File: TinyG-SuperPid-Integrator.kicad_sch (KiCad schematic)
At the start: 16 parts, among them J1 TINYG, J2 SPP, J3 Vin (12-26V), U1 LM2678T-5.0

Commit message: Completed schematic, first Rev of PCB layout complete.
PCB Layout complete
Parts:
- added C2: .1uF, Capacitor_THT:C_Disc_D3.8mm_W2.6mm_P2.50mm, symbol Device:C_Small
- added J4: UJ2-AH-4-TH, 1_MyGlobalLibFootprintLibrary:CUI_UJ2-AH-4-TH, symbol 1_MyGlobalLib:UJ2-AH-4-TH
- added J5: SSR, 1_MyGlobalLibFootprintLibrary:CUI_TB001-500-02BE, symbol 1_MyGlobalLib:TB001-500-02BE
- added R5, R7: 47K, 1_MyGlobalLibFootprintLibrary:MRS25000C2260FCT00, symbol Device:R_Small_US
- added R6: 82K, 1_MyGlobalLibFootprintLibrary:MRS25000C2260FCT00, symbol Device:R_Small_US
- added R8: 38.3K, 1_MyGlobalLibFootprintLibrary:MRS25000C2260FCT00, symbol Device:R_Small_US
- added R9: 226, 1_MyGlobalLibFootprintLibrary:MRS25000C2260FCT00, symbol Device:R_Small_US
- added U3: TLP2662F, 1_MyGlobalLibFootprintLibrary:TLP2662F, symbol 1_MyGlobalLib:TLP2662F
- gave numbers to parts that had none: 1
- renumbered Cb to Cb1, Cin to Cin1, Cinx to Cinx1, Cout to Cout1
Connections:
- net +5V: now also C2.1, J4.1 (Vcc), R6.2, R8.2, U3.8 (Vcc)
- net GND: now also C2.2, J4.4 (GND), J4.5 (SHIELD), J5.2 (-), R5.1, R7.1, R9.1, U3.5 (GND)
- net at J1.3 (COOL): now also U3.4 (A2)
- new net: J4.2 (D-), R5.2, R6.1
- new net: J4.3 (D+), R7.2, R8.1
- new net: J5.1 (+), U3.6 (O2)
- new net: R9.2, U3.3 (C2)
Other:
- note added: "TinyG and SuperPID integration. Converts 3.3V TinyG outputs to 5.0 volt levels. Inverts SPIN command from active low to active high. Has solid state relay output for external actuation of cooling or dust collection. Includes 5V, 4Amp power supply with USB Output for Raspberry pi or other small USB device. Provides 5V power for SuperPID."
- note removed: "TinyG and SuperPID integration. Converts 3.3V TinyG outputs to 5.0 volt levels. Inverts SPIN command from active low to active high. Has relay output for external actuation of cooling or dust collection. Includes 5V, 4Amp power supply with USB Output for Raspberry pi or other small USB device. Provieds 5V power for SuperPID."
- moved on the sheet: Cb1, Cin1, Cinx1, Cout1, D1, J3, L1, U1

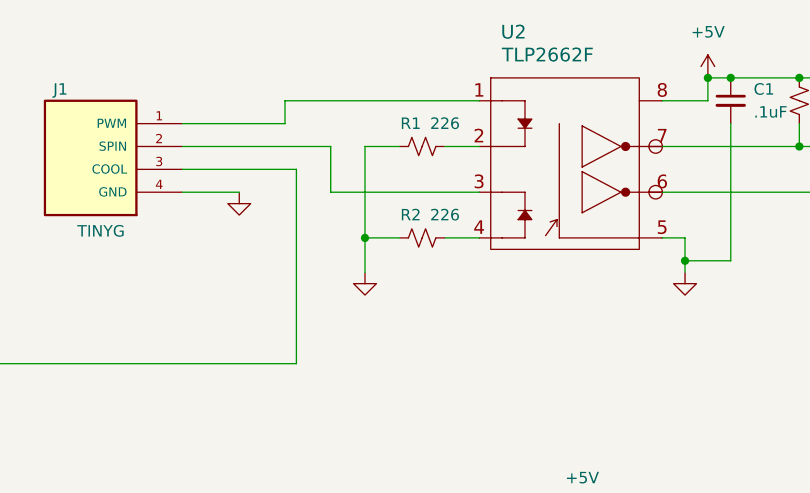
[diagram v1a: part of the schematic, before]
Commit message: Fixed backwards diode on U2, straightened internal plane boundaries (aesthetic)
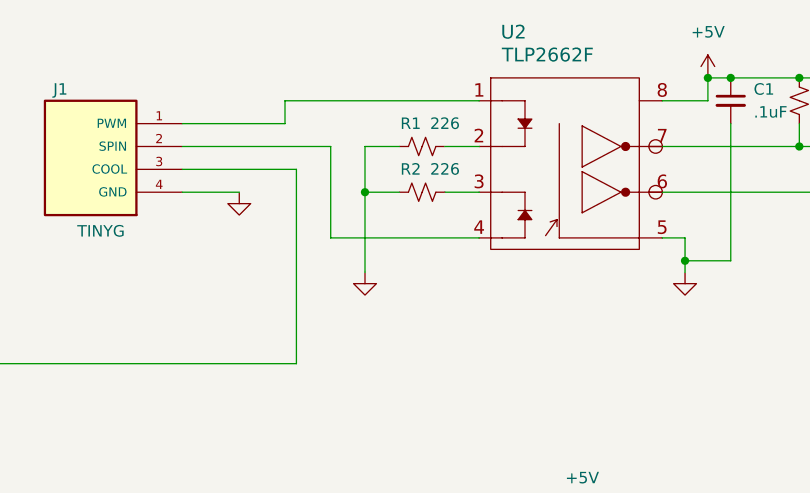
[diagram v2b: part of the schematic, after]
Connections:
- net at U2.3 (C2): now also R2.1; no longer J1.2 (SPIN)
- net at U2.4 (A2): now also J1.2 (SPIN); no longer R2.1
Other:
- moved on the sheet: R2
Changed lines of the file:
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@@
   (junction (at 184.15 113.03) (diameter 0) (color 0 0 0 0)
   )
-  (junction (at 166.37 39.37) (diameter 0) (color 0 0 0 0)
-  )
   (junction (at 170.18 93.98) (diameter 0) (color 0 0 0 0)
   )
@@
   (junction (at 201.93 41.91) (diameter 0) (color 0 0 0 0)
   )
+  (junction (at 166.37 34.29) (diameter 0) (color 0 0 0 0)
+  )
   (junction (at 231.14 93.98) (diameter 0) (color 0 0 0 0)
   )
@@
     (stroke (width 0) (type default) (color 0 0 0 0))
   )
-  (wire (pts (xy 166.37 39.37) (xy 170.18 39.37))
-    (stroke (width 0) (type default) (color 0 0 0 0))
-  )
   (wire (pts (xy 85.09 43.18) (xy 85.09 48.26))
     (stroke (width 0) (type default) (color 0 0 0 0))
@@
     (stroke (width 0) (type default) (color 0 0 0 0))
   )
+  (wire (pts (xy 166.37 34.29) (xy 166.37 43.18))
+    (stroke (width 0) (type default) (color 0 0 0 0))
+  )
   (wire (pts (xy 198.12 113.03) (xy 219.71 113.03))
     (stroke (width 0) (type default) (color 0 0 0 0))
@@
     (stroke (width 0) (type default) (color 0 0 0 0))
   )
-  (wire (pts (xy 162.56 34.29) (xy 179.07 34.29))
-    (stroke (width 0) (type default) (color 0 0 0 0))
-  )
   (wire (pts (xy 81.28 53.34) (xy 90.17 53.34))
     (stroke (width 0) (type default) (color 0 0 0 0))
@@
     (stroke (width 0) (type default) (color 0 0 0 0))
   )
-  (wire (pts (xy 175.26 39.37) (xy 179.07 39.37))
-    (stroke (width 0) (type default) (color 0 0 0 0))
-  )
   (wire (pts (xy 242.57 73.66) (xy 215.9 73.66))
     (stroke (width 0) (type default) (color 0 0 0 0))
@@
     (stroke (width 0) (type default) (color 0 0 0 0))
   )
-  (wire (pts (xy 166.37 29.21) (xy 166.37 39.37))
+  (wire (pts (xy 166.37 29.21) (xy 166.37 34.29))
     (stroke (width 0) (type default) (color 0 0 0 0))
   )
@@
     (stroke (width 0) (type default) (color 0 0 0 0))
   )
-  (wire (pts (xy 166.37 39.37) (xy 166.37 43.18))
-    (stroke (width 0) (type default) (color 0 0 0 0))
-  )
   (wire (pts (xy 96.52 81.28) (xy 113.03 81.28))
     (stroke (width 0) (type default) (color 0 0 0 0))
@@
     (stroke (width 0) (type default) (color 0 0 0 0))
   )
+  (wire (pts (xy 166.37 34.29) (xy 170.18 34.29))
+    (stroke (width 0) (type default) (color 0 0 0 0))
+  )
   (wire (pts (xy 113.03 90.17) (xy 113.03 93.98))
     (stroke (width 0) (type default) (color 0 0 0 0))
@@
     (stroke (width 0) (type default) (color 0 0 0 0))
   )
-  (wire (pts (xy 162.56 29.21) (xy 162.56 34.29))
+  (wire (pts (xy 162.56 29.21) (xy 162.56 39.37))
     (stroke (width 0) (type default) (color 0 0 0 0))
   )
@@
     (stroke (width 0) (type default) (color 0 0 0 0))
   )
+  (wire (pts (xy 179.07 39.37) (xy 162.56 39.37))
+    (stroke (width 0) (type default) (color 0 0 0 0))
+  )
   (wire (pts (xy 207.01 41.91) (xy 201.93 41.91))
     (stroke (width 0) (type default) (color 0 0 0 0))
@@
   )
   (wire (pts (xy 158.75 31.75) (xy 158.75 53.34))
+    (stroke (width 0) (type default) (color 0 0 0 0))
+  )
+  (wire (pts (xy 175.26 34.29) (xy 179.07 34.29))
     (stroke (width 0) (type default) (color 0 0 0 0))
   )
@@
     (pin "2")
   )
-  (symbol (lib_id "Device:R_Small_US") (at 172.72 39.37 270) (unit 1)
-    (in_bom yes) (on_board yes)
-    (property "Reference" "R2" (id 0) (at 171.45 36.83 90))
-    (property "Value" "226" (id 1) (at 175.26 36.83 90))
-    (property "Footprint" "1_MyGlobalLibFootprintLibrary:MRS25000C2260FCT00" (id 2) (at 172.72 39.37 0)
-      (effects (font (size 1.27 1.27)) hide)
-    )
-    (property "Datasheet" "~" (id 3) (at 172.72 39.37 0)
-      (effects (font (size 1.27 1.27)) hide)
-    )
-    (property "Digikey" "BC4072CT-ND" (id 4) (at 172.72 39.37 0)
-      (effects (font (size 1.27 1.27)) hide)
-    )
-    (property "Cost1" ".29" (id 5) (at 172.72 39.37 0)
-      (effects (font (size 1.27 1.27)) hide)
-    )
+  (symbol (lib_id "Device:R_Small_US") (at 172.72 34.29 270) (unit 1)
+    (in_bom yes) (on_board yes)
+    (property "Reference" "R2" (id 0) (at 171.45 31.75 90))
+    (property "Value" "226" (id 1) (at 175.26 31.75 90))
+    (property "Footprint" "1_MyGlobalLibFootprintLibrary:MRS25000C2260FCT00" (id 2) (at 172.72 34.29 0)
+      (effects (font (size 1.27 1.27)) hide)
+    )
+    (property "Datasheet" "~" (id 3) (at 172.72 34.29 0)
+      (effects (font (size 1.27 1.27)) hide)
+    )
+    (property "Digikey" "BC4072CT-ND" (id 4) (at 172.72 34.29 0)
+      (effects (font (size 1.27 1.27)) hide)
+    )
+    (property "Cost1" ".29" (id 5) (at 172.72 34.29 0)
+      (effects (font (size 1.27 1.27)) hide)
+    )

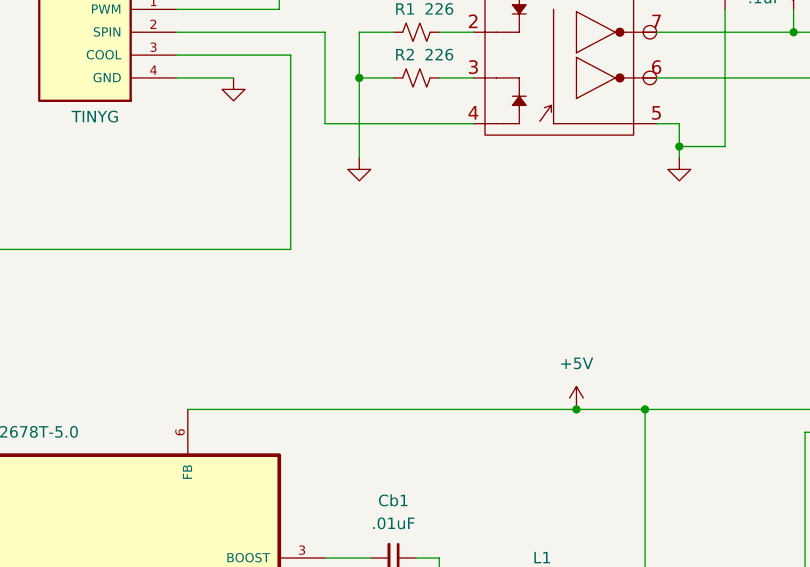
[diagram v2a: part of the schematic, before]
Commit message: Added power LED, load resistor. Updated power supply layout.
Updated layout of power supply to shorten distances between L1, Cout, Cin, and Cb1.  Added power LED indicator and pads for a small load resistor to stabilize the switching PS if needed.
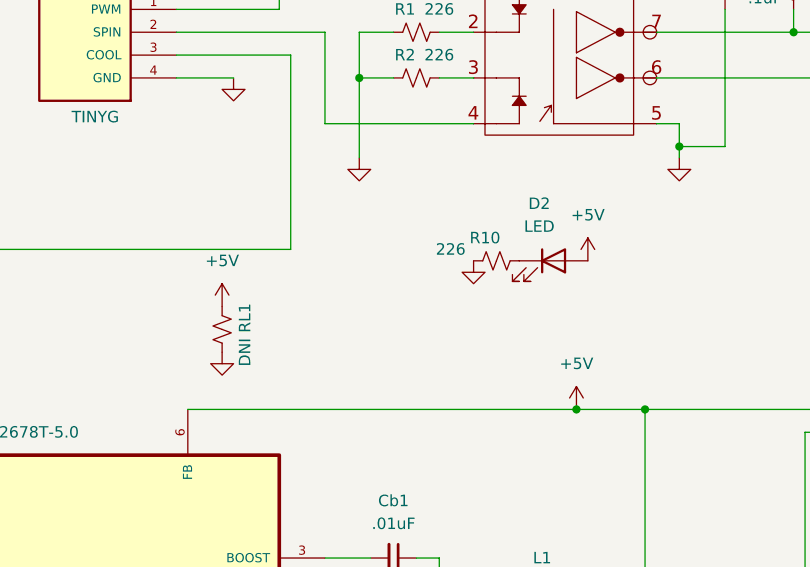
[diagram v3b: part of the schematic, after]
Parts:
- added D2: LED, LED_THT:LED_D5.0mm, symbol Device:LED
- added R10: 226, 1_MyGlobalLibFootprintLibrary:MRS25000C2260FCT00, symbol Device:R_Small_US
- added RL1: DNI, Resistor_THT:R_Axial_DIN0309_L9.0mm_D3.2mm_P12.70mm_Horizontal, symbol Device:R_Small_US
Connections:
- net +5V: now also D2.2 (A), RL1.2
- net GND: now also R10.2, RL1.1
- new net: D2.1 (K), R10.1
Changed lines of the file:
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@@
+    (pin "1")
+  )
+  (symbol (lib_id "power:+5V") (at 191.77 54.61 0) (unit 1)
+    (in_bom yes) (on_board yes) (fields_autoplaced)
+    (property "Reference" "#PWR0116" (id 0) (at 191.77 58.42 0)
+      (effects (font (size 1.27 1.27)) hide)
+    )
+    (property "Value" "+5V" (id 1) (at 191.77 49.53 0))
+    (property "Footprint" "" (id 2) (at 191.77 54.61 0)
+      (effects (font (size 1.27 1.27)) hide)
+    )
+    (property "Datasheet" "" (id 3) (at 191.77 54.61 0)
+      (effects (font (size 1.27 1.27)) hide)
+    )
     (pin "1")
   )
@@
     (pin "1")
   )
+  (symbol (lib_id "Device:R_Small_US") (at 151.13 62.23 180) (unit 1)
+    (in_bom yes) (on_board yes)
+    (property "Reference" "RL1" (id 0) (at 153.67 60.96 90))
+    (property "Value" "DNI" (id 1) (at 153.67 64.77 90))
+    (property "Footprint" "Resistor_THT:R_Axial_DIN0309_L9.0mm_D3.2mm_P12.70mm_Horizontal" (id 2) (at 151.13 62.23 0)
+      (effects (font (size 1.27 1.27)) hide)
+    )
+    (property "Datasheet" "~" (id 3) (at 151.13 62.23 0)
+      (effects (font (size 1.27 1.27)) hide)
+    )
+    (property "Digikey" "BC4072CT-ND" (id 4) (at 151.13 62.23 0)
+      (effects (font (size 1.27 1.27)) hide)
+    )
+    (property "Cost1" ".29" (id 5) (at 151.13 62.23 0)
+      (effects (font (size 1.27 1.27)) hide)
+    )
+    (pin "1")
+    (pin "2")
+  )
   (symbol (lib_name "TB001-500-04BE_1") (lib_id "1_MyGlobalLib:TB001-500-04BE") (at 135.89 31.75 0) (mirror y) (unit 1)
     (in_bom yes) (on_board yes)
@@
     (pin "2")
   )
+  (symbol (lib_id "power:GND") (at 179.07 54.61 0) (unit 1)
+    (in_bom yes) (on_board yes)
+    (property "Reference" "#PWR0113" (id 0) (at 179.07 60.96 0)
+      (effects (font (size 1.27 1.27)) hide)
+    )
+    (property "Value" "GND" (id 1) (at 182.88 57.15 0)
+      (effects (font (size 1.27 1.27)) hide)
+    )
+    (property "Footprint" "" (id 2) (at 179.07 54.61 0)
+      (effects (font (size 1.27 1.27)) hide)
+    )
+    (property "Datasheet" "" (id 3) (at 179.07 54.61 0)
+      (effects (font (size 1.27 1.27)) hide)
+    )
+    (pin "1")
+  )
+  (symbol (lib_id "Device:LED") (at 187.96 54.61 0) (unit 1)
+    (in_bom yes) (on_board yes) (fields_autoplaced)
+    (property "Reference" "D2" (id 0) (at 186.3725 48.26 0))
+    (property "Value" "LED" (id 1) (at 186.3725 50.8 0))
+    (property "Footprint" "LED_THT:LED_D5.0mm" (id 2) (at 187.96 54.61 0)
+      (effects (font (size 1.27 1.27)) hide)
+    )
+    (property "Datasheet" "~" (id 3) (at 187.96 54.61 0)
+      (effects (font (size 1.27 1.27)) hide)
+    )
+    (pin "1")
+    (pin "2")
+  )
+  (symbol (lib_id "Device:R_Small_US") (at 181.61 54.61 270) (unit 1)
+    (in_bom yes) (on_board yes)
+    (property "Reference" "R10" (id 0) (at 180.34 52.07 90))
+    (property "Value" "226" (id 1) (at 176.53 53.34 90))
+    (property "Footprint" "1_MyGlobalLibFootprintLibrary:MRS25000C2260FCT00" (id 2) (at 181.61 54.61 0)
+      (effects (font (size 1.27 1.27)) hide)
+    )
+    (property "Datasheet" "~" (id 3) (at 181.61 54.61 0)
+      (effects (font (size 1.27 1.27)) hide)
+    )
+    (property "Digikey" "BC4072CT-ND" (id 4) (at 181.61 54.61 0)
+      (effects (font (size 1.27 1.27)) hide)
+    )
+    (property "Cost1" ".29" (id 5) (at 181.61 54.61 0)
+      (effects (font (size 1.27 1.27)) hide)
+    )
+    (pin "1")
+    (pin "2")
+  )
   (symbol (lib_id "Device:C_Small") (at 170.18 87.63 270) (unit 1)
     (in_bom yes) (on_board yes) (fields_autoplaced)
@@
     (pin "2")
   )
+  (symbol (lib_id "power:GND") (at 151.13 64.77 0) (unit 1)
+    (in_bom yes) (on_board yes)
+    (property "Reference" "#PWR0114" (id 0) (at 151.13 71.12 0)
+      (effects (font (size 1.27 1.27)) hide)
+    )
+    (property "Value" "GND" (id 1) (at 154.94 67.31 0)
+      (effects (font (size 1.27 1.27)) hide)
+    )
+    (property "Footprint" "" (id 2) (at 151.13 64.77 0)
+      (effects (font (size 1.27 1.27)) hide)
+    )
+    (property "Datasheet" "" (id 3) (at 151.13 64.77 0)
+      (effects (font (size 1.27 1.27)) hide)
+    )
+    (pin "1")
+  )
   (symbol (lib_id "Device:L") (at 186.69 93.98 90) (unit 1)
     (in_bom yes) (on_board yes) (fields_autoplaced)
@@
     (pin "1")
     (pin "2")
+  )
+  (symbol (lib_id "power:+5V") (at 151.13 59.69 0) (unit 1)
+    (in_bom yes) (on_board yes) (fields_autoplaced)
+    (property "Reference" "#PWR0115" (id 0) (at 151.13 63.5 0)
+      (effects (font (size 1.27 1.27)) hide)
+    )
+    (property "Value" "+5V" (id 1) (at 151.13 54.61 0))
+    (property "Footprint" "" (id 2) (at 151.13 59.69 0)
+      (effects (font (size 1.27 1.27)) hide)
+    )
+    (property "Datasheet" "" (id 3) (at 151.13 59.69 0)
+      (effects (font (size 1.27 1.27)) hide)
+    )
+    (pin "1")
   )
   (symbol (lib_id "1_MyGlobalLib:TB001-500-04BE") (at 250.19 31.75 0) (unit 1)
@@
       (reference "#PWR0112") (unit 1) (value "GND") (footprint "")
     )
+    (path "/cb90122c-f5e9-48d7-8eaa-0fbfc19cd3a2"
+      (reference "#PWR0113") (unit 1) (value "GND") (footprint "")
+    )
+    (path "/dd71be71-78f5-438a-894f-581fdd42e45a"
+      (reference "#PWR0114") (unit 1) (value "GND") (footprint "")
+    )
+    (path "/eb3f0768-2a83-4348-9892-8a4d41c19d6c"
+      (reference "#PWR0115") (unit 1) (value "+5V") (footprint "")
+    )
+    (path "/1a882f23-bdf3-4095-b035-263a39583163"
+      (reference "#PWR0116") (unit 1) (value "+5V") (footprint "")
+    )
     (path "/c2ae2e2c-4f5d-4076-bad6-26f0a630e122"
       (reference "C1") (unit 1) (value ".1uF") (footprint "Capacitor_THT:C_Disc_D3.8mm_W2.6mm_P2.50mm")
@@
       (reference "D1") (unit 1) (value "12TQ200") (footprint "Package_TO_SOT_THT:TO-220-2_Vertical")
     )
+    (path "/d49d5d72-36df-43ca-96b7-823c0e3191f9"
+      (reference "D2") (unit 1) (value "LED") (footprint "LED_THT:LED_D5.0mm")
+    )
     (path "/b67fe498-1f40-409f-aac2-758d99911594"
       (reference "J1") (unit 1) (value "TINYG") (footprint "1_MyGlobalLibFootprintLibrary:CUI_TB001-500-04BE")
@@
       (reference "R9") (unit 1) (value "226") (footprint "1_MyGlobalLibFootprintLibrary:MRS25000C2260FCT00")
     )
+    (path "/d504e8c0-4c18-477e-bf61-81b8b95d11e9"
+      (reference "R10") (unit 1) (value "226") (footprint "1_MyGlobalLibFootprintLibrary:MRS25000C2260FCT00")
+    )
+    (path "/b0f0de1d-e113-4576-8c13-7526ff7ab898"
+      (reference "RL1") (unit 1) (value "DNI") (footprint "Resistor_THT:R_Axial_DIN0309_L9.0mm_D3.2mm_P12.70mm_Horizontal")
+    )
     (path "/f434dfac-4b58-41f0-9220-4db4b5853ca2"
